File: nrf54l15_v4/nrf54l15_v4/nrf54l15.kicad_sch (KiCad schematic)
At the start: 16 parts, among them U6 nRF54L15-QFXX, X1 XL7EL89CKI-111YLC-32M

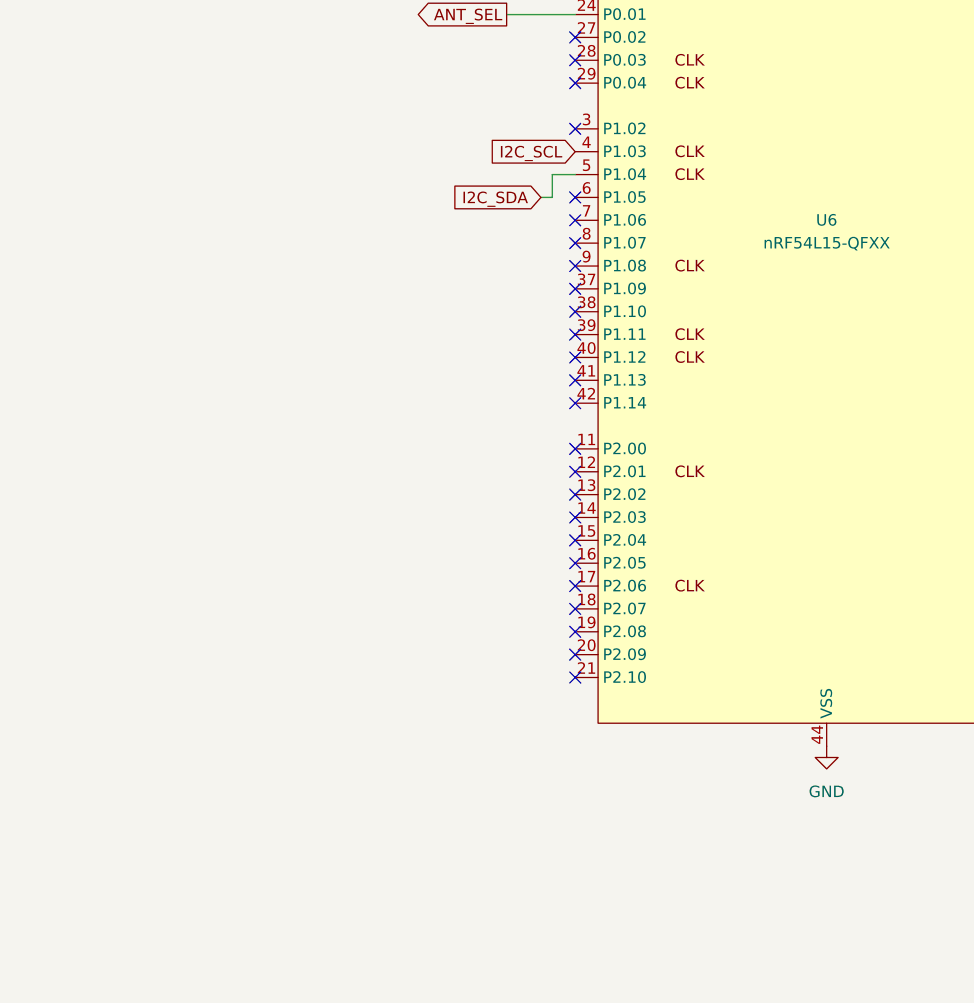
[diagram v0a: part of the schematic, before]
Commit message: Update nrf54l15_v4 design; add feather board, enclosure, and docs
nrf54l15_v4:
- Sensor connector (CN1) reworked to a 14-pin Molex 503480-1400 FFC
  connector with a project footprint library (nrf54l15_v4.pretty) and
  vendor drawing/3D model.
- nRF54L15 pin assignment fixes for the sensor bus (I2C, SPI/UART, INT,
  AIN, board-ID).
- AEM10330 solar block: EN_SLEEP tied to GND, MPPT ratio set to 70%,
  MPNs added to C40-C43.
- Annotation cleanup across antenna, npm1300 and power_supply sheets;
  PCB updated from schematic; zone min clearance set to 0.5 mm.
- Add 3D-printable enclosure generator and STL outputs.

New:
- nrf54l15_feather KiCad project.
- Sensor_Boards/Conductivity_Salinity design notes.
- solar-analysis-v4.md and v4-sensor-connector.md design docs.
- AEM10330 and PowerFilm LL200-2.4-75 datasheets.

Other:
- nrf54l15_v2 BOM: fix misplaced capacitance value columns (C9/C11);
  add .xlsx BOM.
- .gitignore: ignore dated schematic backups, extra claude_bak copies,
  vendor zip downloads and DRC report exports.

Co-Authored-By: Claude Opus 5.5 <noreply@anthropic.com>
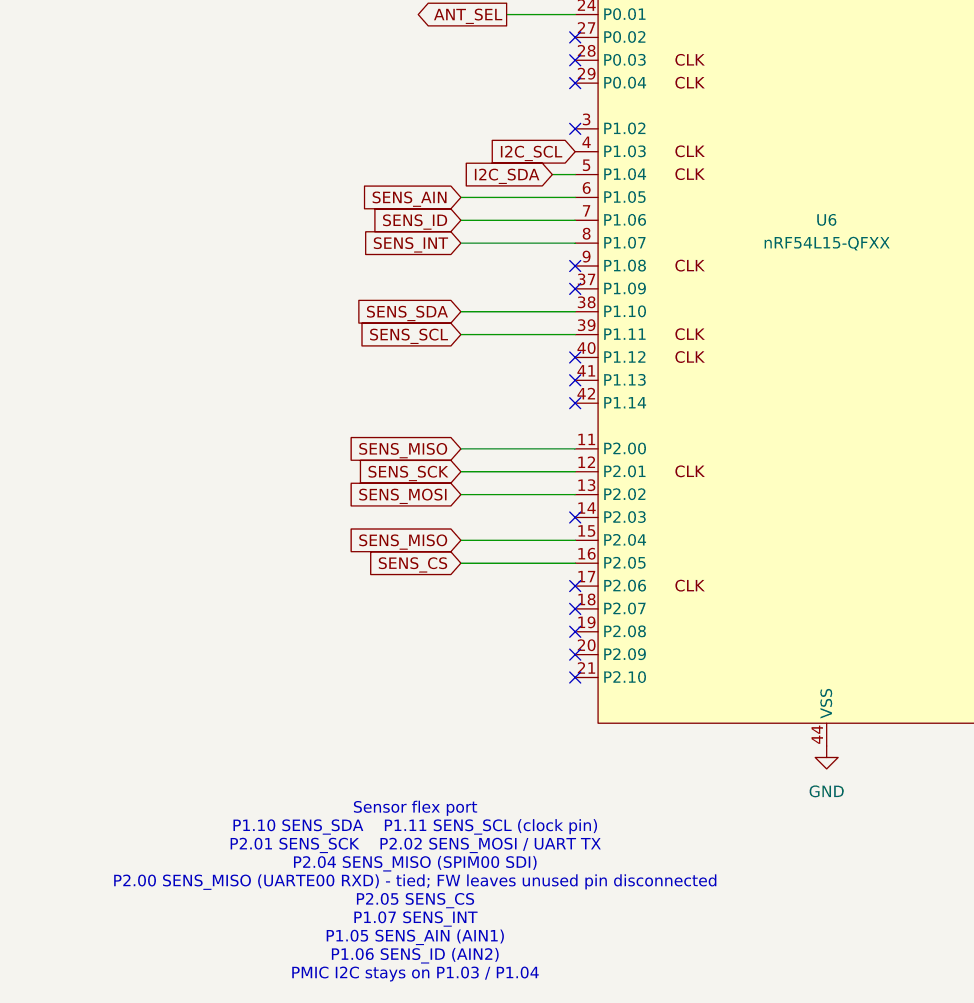
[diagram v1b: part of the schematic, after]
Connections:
- net SENS_MISO: now reaches U6.11 (P2.00)
- net SENS_MISO: now also U6.15 (P2.04)
- net SENS_SCK: now reaches U6.12 (P2.01)
- net SENS_MOSI: now reaches U6.13 (P2.02)
- net SENS_CS: now reaches U6.16 (P2.05)
- net SENS_SDA: now reaches U6.38 (P1.10)
- net SENS_SCL: now reaches U6.39 (P1.11)
- net SENS_AIN: now reaches U6.6 (P1.05)
- net SENS_ID: now reaches U6.7 (P1.06)
- net SENS_INT: now reaches U6.8 (P1.07)
- no-connect marks 25 -> 15
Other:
- note added: "Sensor flex port P1.10 SENS_SDA P1.11 SENS_SCL (clock pin) P2.01 SENS_SCK P2.02 SENS_MOSI / UART TX P2.04 SENS_MISO (SPIM00 SDI) P2.00 SENS_MISO (UARTE00 RXD) - tied; FW leaves unused pin disconnected P2.05 SENS_CS P1.07 SENS_INT P1.05 SENS_AIN (AIN1) P1.06 SENS_ID (AIN2) PMIC I2C stays on P1.03 / P1.04"
